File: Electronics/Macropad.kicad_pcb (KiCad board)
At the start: 2 copper layers, 114.5 x 142.3 mm, 45 parts, among them SW1 CherryMX, SW10 CherryMX, SW11 CherryMX, SW12 CherryMX, SW13 CherryMX, SW14 CherryMX, SW15 CherryMX, SW16 CherryMX, SW17 CherryMX, SW18 CherryMX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

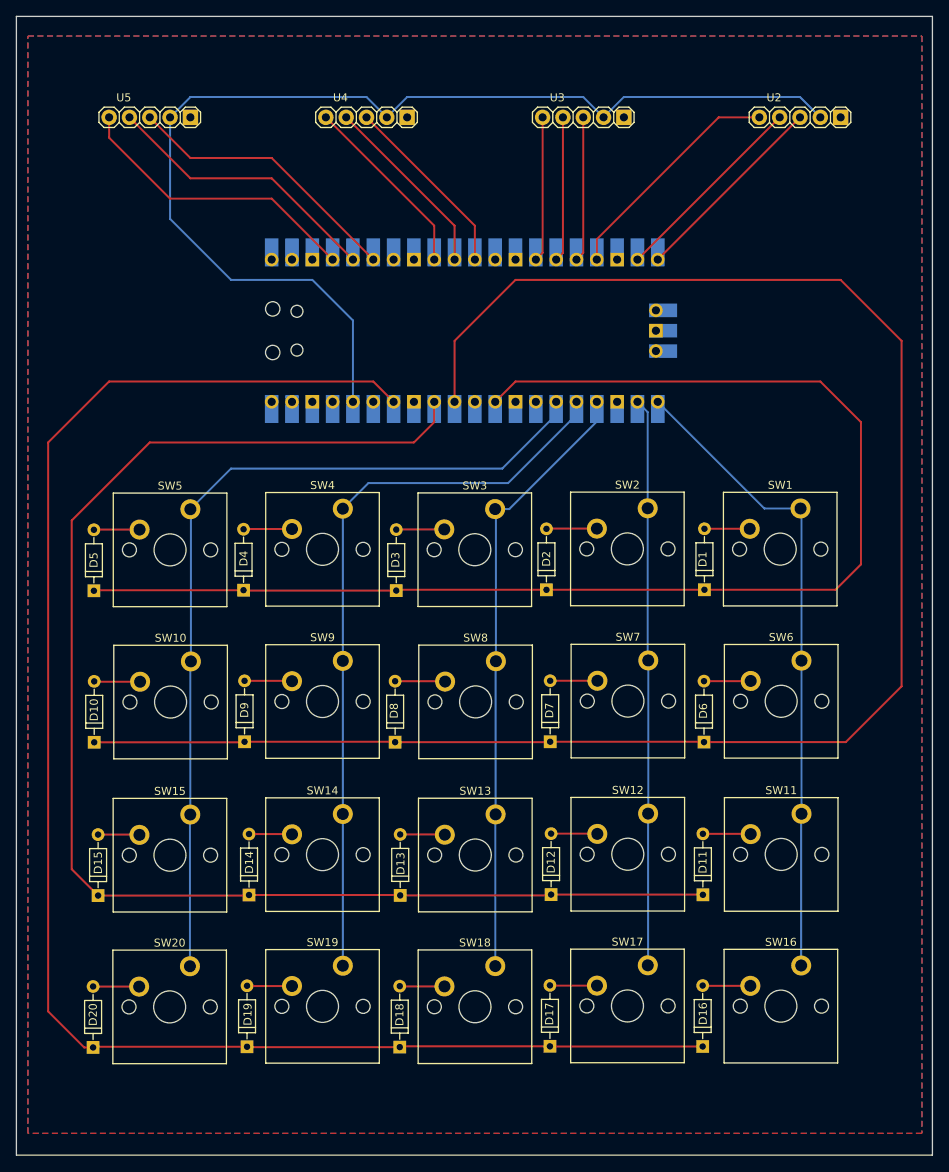
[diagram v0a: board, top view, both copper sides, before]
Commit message: Removed Gerbers, fixed row/column diode inversion
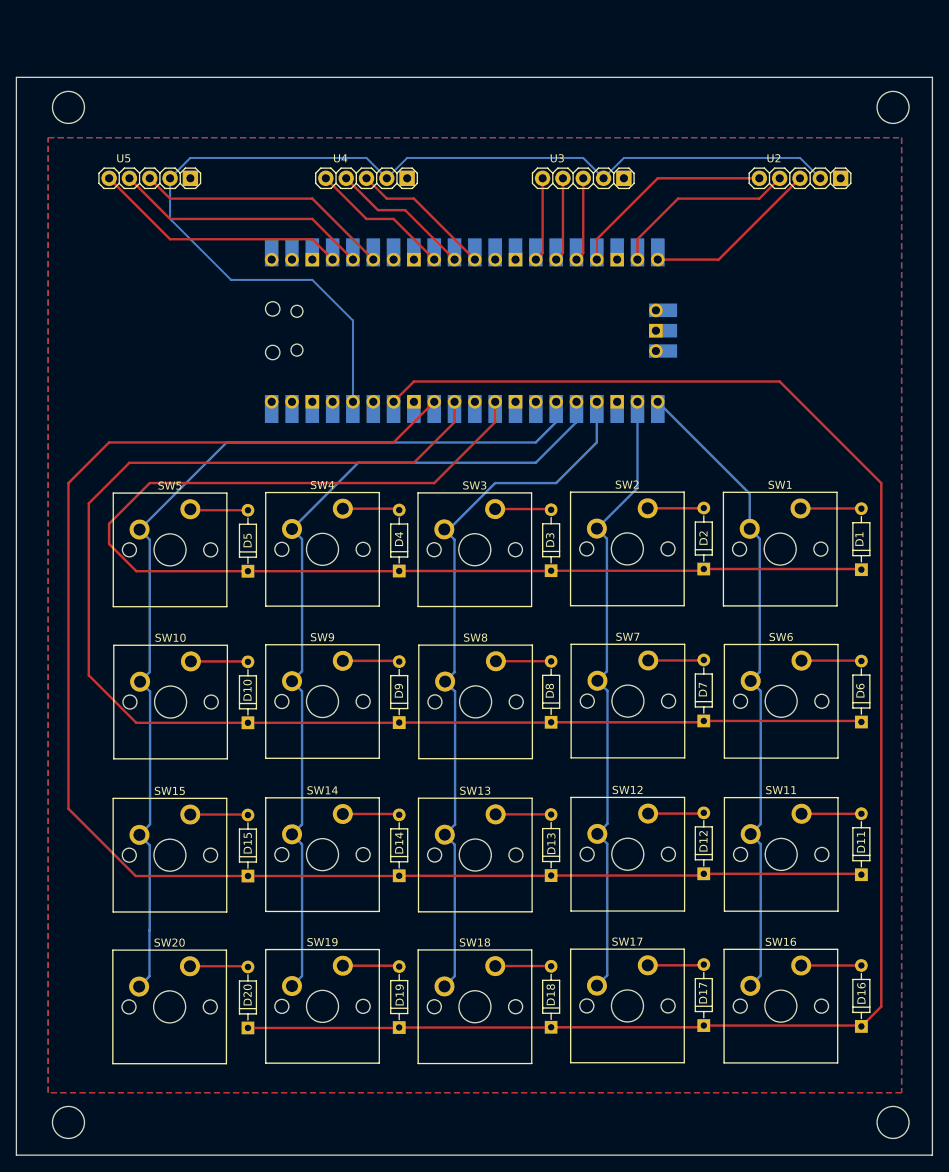
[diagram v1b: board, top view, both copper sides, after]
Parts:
- moved D16 20.0 mm to (127.1, 165.7)
- moved D11 20.0 mm to (127.1, 146.7)
- moved D2 19.8 mm to (107.4, 108.5)
- moved D6 19.8 mm to (127.1, 127.7)
- moved D1 19.8 mm to (127.1, 108.6)
- moved D8 19.7 mm to (88.3, 127.7)
- moved D4 19.6 mm to (69.3, 108.8)
- moved D3 19.5 mm to (88.3, 108.7)
- moved D20 19.5 mm to (50.4, 165.9)
- moved D9 19.5 mm to (69.3, 127.7)
- moved D5 19.4 mm to (50.4, 108.8)
- moved D17 19.4 mm to (107.4, 165.6)
- moved D7 19.4 mm to (107.4, 127.5)
- moved D10 19.4 mm to (50.4, 127.8)
- moved D12 19.3 mm to (107.4, 146.6)
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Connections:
- SW1 pad 1: Net-(D1-A) -> /MTX_COL_1
- SW1 pad 2: /MTX_COL_1 -> Net-(D1-A)
- SW10 pad 1: Net-(D10-A) -> /MTX_COL_5
- SW10 pad 2: /MTX_COL_5 -> Net-(D10-A)
- SW11 pad 1: Net-(D11-A) -> /MTX_COL_1
- SW11 pad 2: /MTX_COL_1 -> Net-(D11-A)
- SW12 pad 1: Net-(D12-A) -> /MTX_COL_2
- SW12 pad 2: /MTX_COL_2 -> Net-(D12-A)
- SW13 pad 1: Net-(D13-A) -> /MTX_COL_3
- SW13 pad 2: /MTX_COL_3 -> Net-(D13-A)
- SW14 pad 1: Net-(D14-A) -> /MTX_COL_4
- SW14 pad 2: /MTX_COL_4 -> Net-(D14-A)
- SW15 pad 1: Net-(D15-A) -> /MTX_COL_5
- SW15 pad 2: /MTX_COL_5 -> Net-(D15-A)
- SW16 pad 1: Net-(D16-A) -> /MTX_COL_1
- SW16 pad 2: /MTX_COL_1 -> Net-(D16-A)
- SW17 pad 1: Net-(D17-A) -> /MTX_COL_2
- SW17 pad 2: /MTX_COL_2 -> Net-(D17-A)
- SW18 pad 1: Net-(D18-A) -> /MTX_COL_3
- SW18 pad 2: /MTX_COL_3 -> Net-(D18-A)
- SW19 pad 1: Net-(D19-A) -> /MTX_COL_4
- SW19 pad 2: /MTX_COL_4 -> Net-(D19-A)
- SW2 pad 1: Net-(D2-A) -> /MTX_COL_2
- SW2 pad 2: /MTX_COL_2 -> Net-(D2-A)
- SW20 pad 1: Net-(D20-A) -> /MTX_COL_5
- SW20 pad 2: /MTX_COL_5 -> Net-(D20-A)
- SW3 pad 1: Net-(D3-A) -> /MTX_COL_3
- SW3 pad 2: /MTX_COL_3 -> Net-(D3-A)
- SW4 pad 1: Net-(D4-A) -> /MTX_COL_4
- SW4 pad 2: /MTX_COL_4 -> Net-(D4-A)
- SW5 pad 1: Net-(D5-A) -> /MTX_COL_5
- SW5 pad 2: /MTX_COL_5 -> Net-(D5-A)
- SW6 pad 1: Net-(D6-A) -> /MTX_COL_1
- SW6 pad 2: /MTX_COL_1 -> Net-(D6-A)
- SW7 pad 1: Net-(D7-A) -> /MTX_COL_2
- SW7 pad 2: /MTX_COL_2 -> Net-(D7-A)
- SW8 pad 1: Net-(D8-A) -> /MTX_COL_3
- SW8 pad 2: /MTX_COL_3 -> Net-(D8-A)
- SW9 pad 1: Net-(D9-A) -> /MTX_COL_4
- SW9 pad 2: /MTX_COL_4 -> Net-(D9-A)
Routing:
- net /MTX_ROW_2: track 216.9 -> 173.1 mm
- net /MTX_ROW_3: track 176.9 -> 193.4 mm
- net /MTX_COL_3: track 76.9 -> 88.9 mm
- net /MTX_COL_4: track 92.8 -> 103.9 mm
- net /MTX_COL_5: track 109.4 -> 120.5 mm
- net /MTX_ROW_4: track 202.3 -> 213.1 mm
- net /MTX_ROW_1: track 164.0 -> 154.5 mm
- net /3V3: track 138.6 -> 131.0 mm
- net /U3_SW: track 18.1 -> 10.5 mm
- net /U3_DT: track 18.1 -> 10.5 mm
- net /U3_CLK: track 18.1 -> 10.5 mm
- net /MTX_COL_2: track 71.0 -> 78.2 mm
- net /U4_SW: track 23.4 -> 17.8 mm
- net /U4_DT: track 23.4 -> 17.8 mm
- net /U4_CLK: track 23.4 -> 17.8 mm
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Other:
- board size 114.5 x 142.3 mm -> 114.5 x 134.7 mm
